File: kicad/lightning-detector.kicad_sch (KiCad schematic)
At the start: 12 parts, among them J1 PWR, J2 TFT LCD Display, J3 Conn_01x03, J4 ADF7020 Breakout, U3 TPS61023DRLR

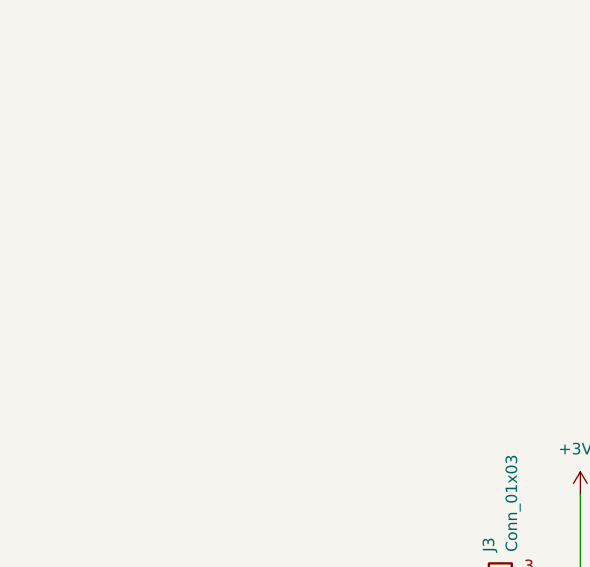
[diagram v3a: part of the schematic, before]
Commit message: add mounting holes
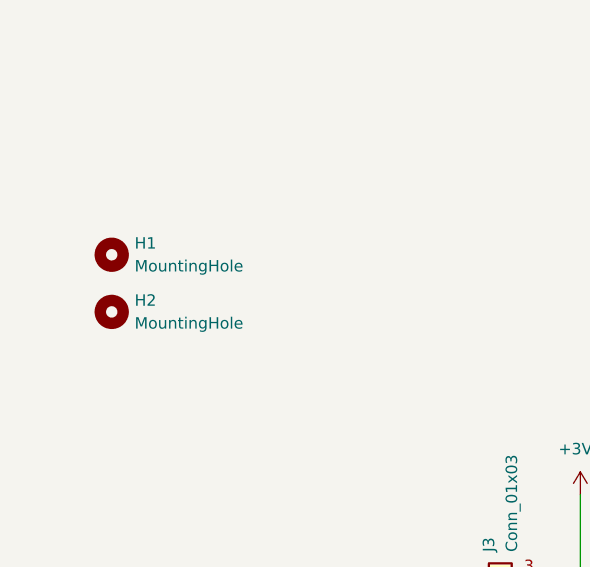
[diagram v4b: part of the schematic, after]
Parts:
- added H1, H2: MountingHole, MountingHole:MountingHole_2.7mm_M2.5, symbol Mechanical:MountingHole
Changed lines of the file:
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@@
+	)
+	(symbol
+		(lib_id "Mechanical:MountingHole")
+		(at 22.86 121.92 0)
+		(unit 1)
+		(exclude_from_sim yes)
+		(in_bom no)
+		(on_board yes)
+		(dnp no)
+		(fields_autoplaced yes)
+		(property "Reference" "H1"
+			(at 25.4 120.6499 0)
+			(effects
+				(font
+					(size 1.27 1.27)
+				)
+				(justify left)
+			)
+		)
+		(property "Value" "MountingHole"
+			(at 25.4 123.1899 0)
+			(effects
+				(font
+					(size 1.27 1.27)
+				)
+				(justify left)
+			)
+		)
+		(property "Footprint" "MountingHole:MountingHole_2.7mm_M2.5"
+			(at 22.86 121.92 0)
+			(effects
+				(font
+					(size 1.27 1.27)
+				)
+				(hide yes)
+			)
+		)
+		(property "Datasheet" "~"
+			(at 22.86 121.92 0)
+			(effects
+				(font
+					(size 1.27 1.27)
+				)
+				(hide yes)
+			)
+		)
+		(property "Description" "Mounting Hole without connection"
+			(at 22.86 121.92 0)
+			(effects
+				(font
+					(size 1.27 1.27)
+				)
+				(hide yes)
+			)
+		)
+		(instances
+			(project ""
+				(path "/b7ef5f28-89c3-4fdc-9151-94fe5013dbaa"
+					(reference "H1")
+					(unit 1)
+				)
+			)
+		)
 	)
 	(symbol
@@
 					(unit 1)
 				)
+			)
+		)
+	)
+	(symbol
+		(lib_id "Mechanical:MountingHole")
+		(at 22.86 128.27 0)
+		(unit 1)
+		(exclude_from_sim yes)
+		(in_bom no)
+		(on_board yes)
+		(dnp no)
+		(fields_autoplaced yes)
+		(property "Reference" "H2"
+			(at 25.4 126.9999 0)
+			(effects
+				(font
+					(size 1.27 1.27)
+				)
+				(justify left)
+			)
+		)
+		(property "Value" "MountingHole"
+			(at 25.4 129.5399 0)
+			(effects
+				(font
+					(size 1.27 1.27)
+				)
+				(justify left)
+			)
+		)
+		(property "Footprint" "MountingHole:MountingHole_2.7mm_M2.5"
+			(at 22.86 128.27 0)
+			(effects
+				(font
+					(size 1.27 1.27)
+				)
+				(hide yes)
+			)
+		)
+		(property "Datasheet" "~"
+			(at 22.86 128.27 0)
+			(effects
+				(font
+					(size 1.27 1.27)
+				)
+				(hide yes)
+			)
+		)
+		(property "Description" "Mounting Hole without connection"
+			(at 22.86 128.27 0)
+			(effects
+				(font
+					(size 1.27 1.27)
+				)
+				(hide yes)
+			)
+		)
+		(instances
+			(project "lightning-detector"
+				(path "/b7ef5f28-89c3-4fdc-9151-94fe5013dbaa"
+					(reference "H2")
+					(unit 1)
+				)
